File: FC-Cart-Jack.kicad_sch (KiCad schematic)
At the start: 5 parts, among them J1 ToCartridge, J2 ToConsole, J3 AudioJack3_SwitchTR, U1 LM321

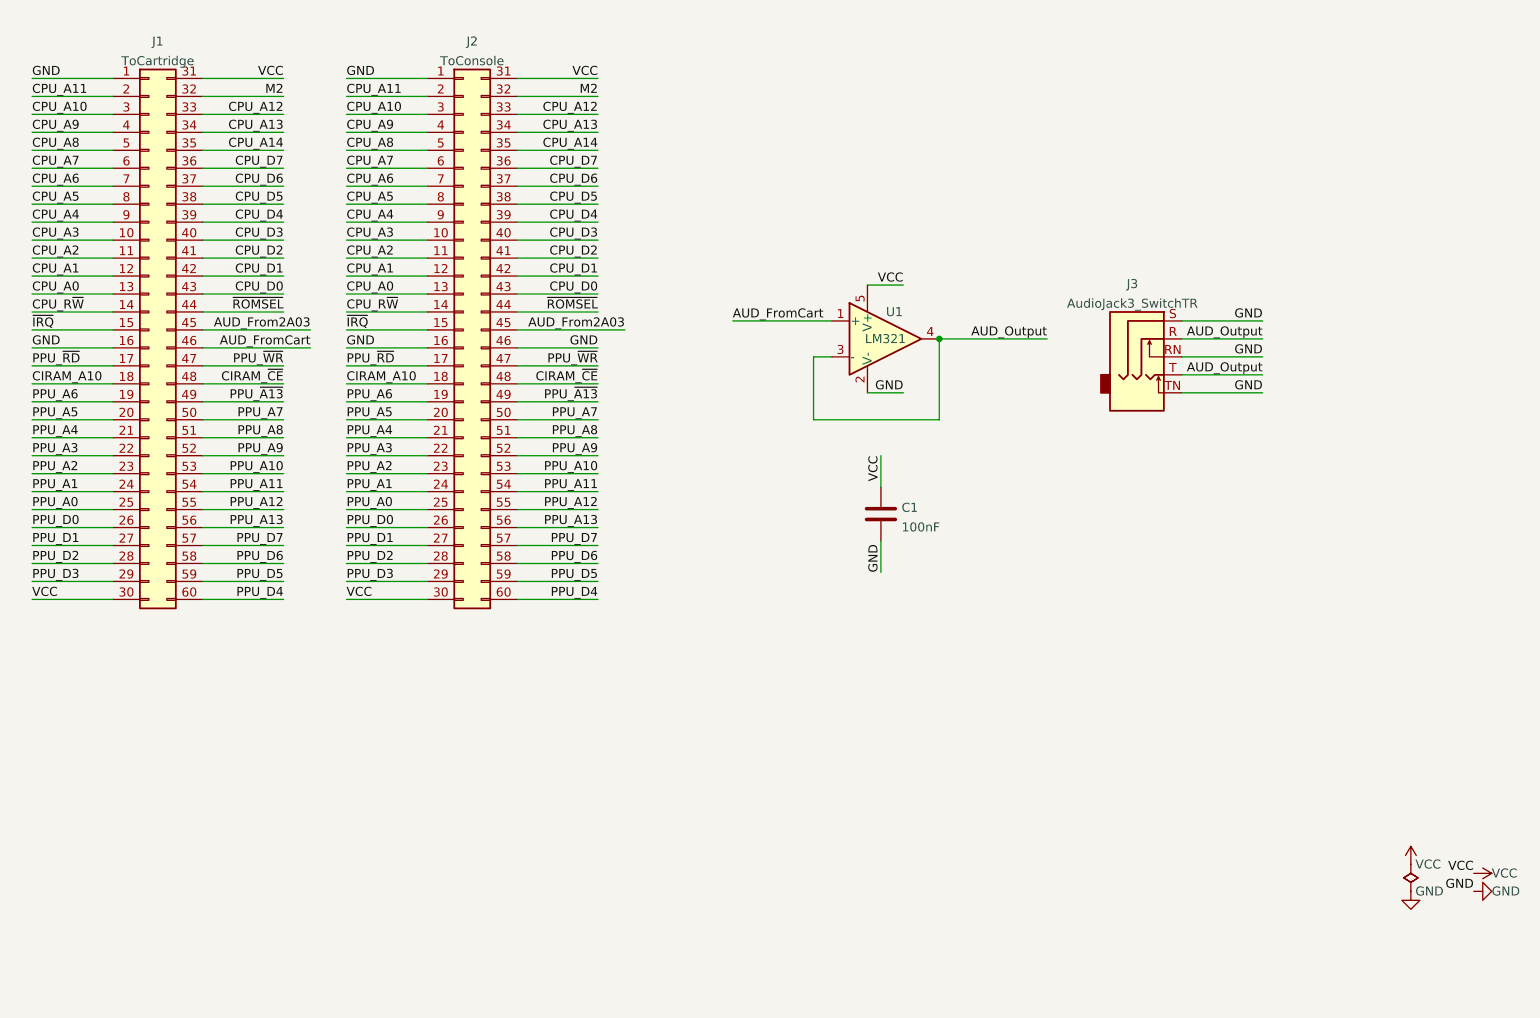
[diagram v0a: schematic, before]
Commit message: Update to KiCad 6.0
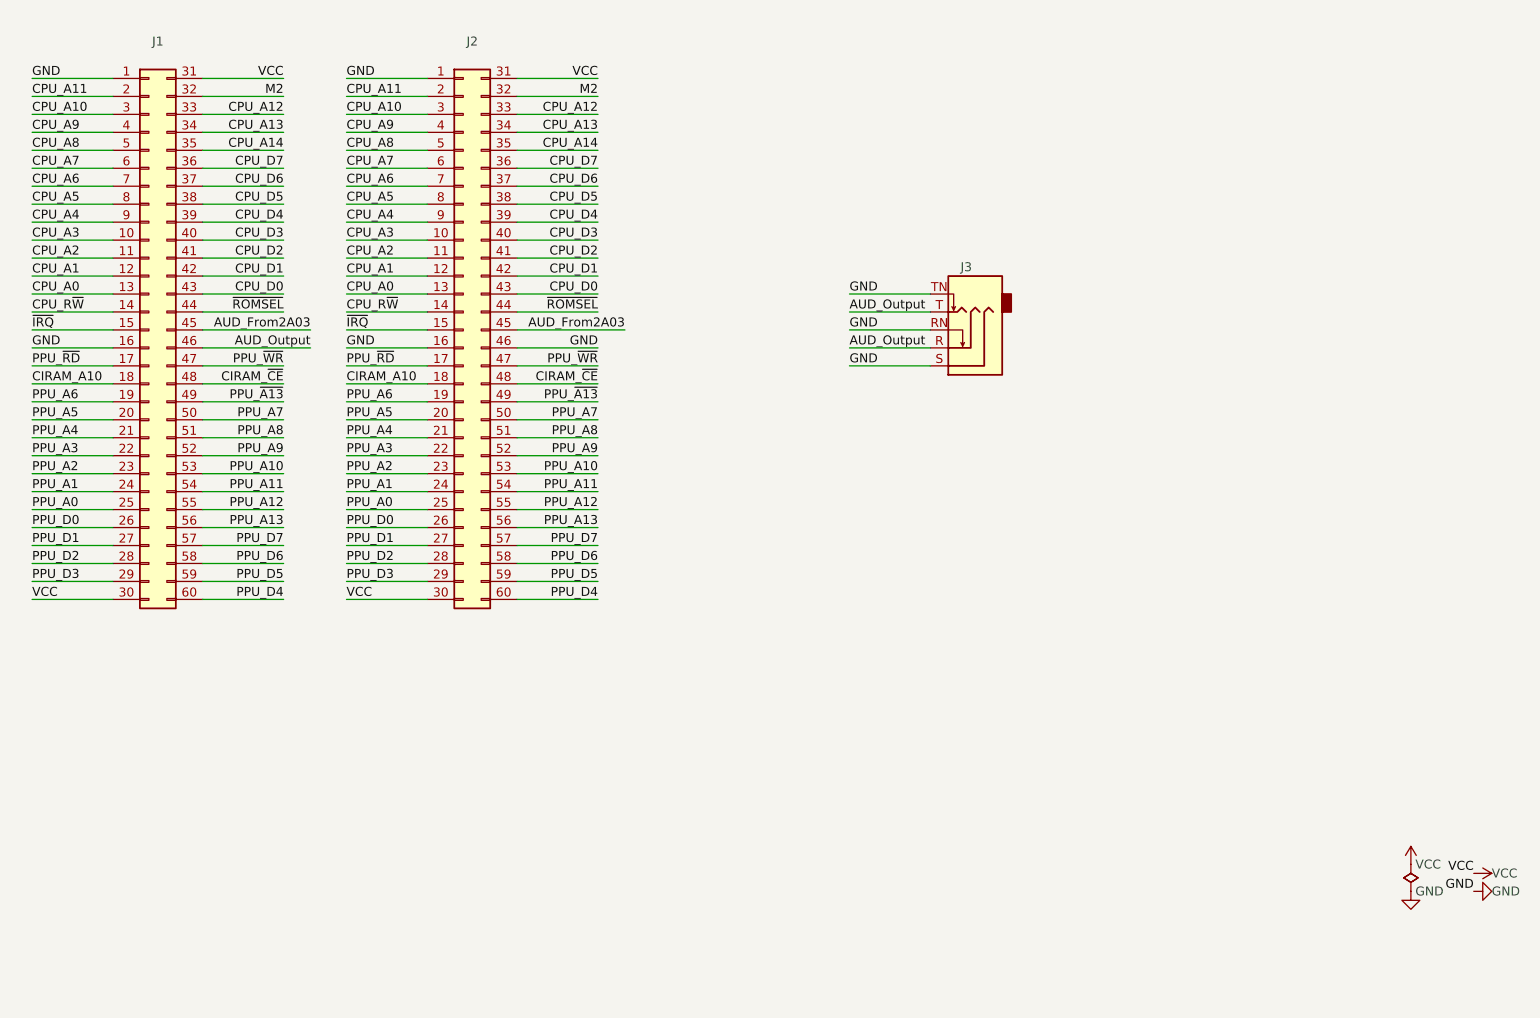
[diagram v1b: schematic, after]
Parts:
- removed C1: 100nF, Capacitor_SMD:C_0805_2012Metric, symbol Device:C
- removed U1: LM321, Package_TO_SOT_SMD:SOT-23-5, symbol Amplifier_Operational:LM321
- J1: value ToCartridge -> (none); footprint custom footprints:card edge -> (none)
- J2: value ToConsole -> (none); footprint custom footprints:HVC-TGROM-01 -> (none)
- J3: value AudioJack3_SwitchTR -> (none); footprint custom footprints:SJ1-3524NG -> (none)
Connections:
- net AUD_FromCart is gone; now on net AUD_Output: J1.46 (Pin_46)
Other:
- moved on the sheet: J3

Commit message: Leave audio out floating
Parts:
- J1: value (none) -> ToCartridge; footprint (none) -> FC-Cart-Jack:card edge
- J2: value (none) -> ToConsole; footprint (none) -> FC-Cart-Jack:HVC-TGROM-01
- J3: value (none) -> ~; footprint (none) -> FC-Cart-Jack:SJ1-3524NG
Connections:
- net GND: no longer J2.46 (Pin_46)
- net AUD_From2A03 renamed AUD_2A03
- no-connect marks 0 -> 1
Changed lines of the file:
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@@
   (title_block
     (title "FC Cartridge Audio Jack")
-    (date "2022-08-13")
-    (rev "0.0.4")
+    (date "2022-11-14")
+    (rev "0.0.5")
     (company "Persune")
   )
+  (no_connect (at 97.79 60.96))
   (wire (pts (xy 17.78 73.66) (xy 29.21 73.66))
     (stroke (width 0) (type default) (color 0 0 0 0))
   )
+  (wire (pts (xy 41.91 58.42) (xy 53.34 58.42))
+    (stroke (width 0) (type default) (color 0 0 0 0))
+  )
   (wire (pts (xy 17.78 71.12) (xy 29.21 71.12))
     (stroke (width 0) (type default) (color 0 0 0 0))
@@
     (stroke (width 0) (type default) (color 0 0 0 0))
   )
+  (wire (pts (xy 86.36 58.42) (xy 97.79 58.42))
+    (stroke (width 0) (type default) (color 0 0 0 0))
+  )
   (wire (pts (xy 62.23 53.34) (xy 73.66 53.34))
     (stroke (width 0) (type default) (color 0 0 0 0))
   )
-  (wire (pts (xy 86.36 58.42) (xy 101.6 58.42))
-    (stroke (width 0) (type default) (color 0 0 0 0))
-  )
   (wire (pts (xy 144.78 55.88) (xy 133.35 55.88))
     (stroke (width 0) (type default) (color 0 0 0 0))
@@
     (stroke (width 0) (type default) (color 0 0 0 0))
   )
-  (wire (pts (xy 41.91 60.96) (xy 57.15 60.96))
-    (stroke (width 0) (type default) (color 0 0 0 0))
-  )
   (wire (pts (xy 41.91 63.5) (xy 53.34 63.5))
     (stroke (width 0) (type default) (color 0 0 0 0))
@@
     (stroke (width 0) (type default) (color 0 0 0 0))
   )
-  (wire (pts (xy 41.91 58.42) (xy 57.15 58.42))
-    (stroke (width 0) (type default) (color 0 0 0 0))
-  )
   (wire (pts (xy 62.23 78.74) (xy 73.66 78.74))
     (stroke (width 0) (type default) (color 0 0 0 0))
@@
     (stroke (width 0) (type default) (color 0 0 0 0))
   )
+  (wire (pts (xy 41.91 60.96) (xy 53.34 60.96))
+    (stroke (width 0) (type default) (color 0 0 0 0))
+  )
   (wire (pts (xy 17.78 43.18) (xy 29.21 43.18))
     (stroke (width 0) (type default) (color 0 0 0 0))
@@
     (effects (font (size 1.27 1.27)) (justify right bottom))
   )
-  (label "AUD_From2A03" (at 101.6 58.42 180)
+  (label "AUD_2A03" (at 97.79 58.42 180)
     (effects (font (size 1.27 1.27)) (justify right bottom))
   )
@@
     (effects (font (size 1.27 1.27)) (justify left bottom))
   )
-  (label "AUD_From2A03" (at 57.15 58.42 180)
+  (label "AUD_2A03" (at 53.34 58.42 180)
     (effects (font (size 1.27 1.27)) (justify right bottom))
   )
@@
     (effects (font (size 1.27 1.27)) (justify left bottom))
   )
-  (label "AUD_Output" (at 57.15 60.96 180)
+  (label "AUD_Output" (at 53.34 60.96 180)
     (effects (font (size 1.27 1.27)) (justify right bottom))
   )
@@
   (label "PPU_A4" (at 17.78 73.66 0)
     (effects (font (size 1.27 1.27)) (justify left bottom))
-  )
-  (label "GND" (at 97.79 60.96 180)
-    (effects (font (size 1.27 1.27)) (justify right bottom))
   )
   (label "VCC" (at 53.34 22.86 180)
@@
     (in_bom yes) (on_board yes) (fields_autoplaced)
     (property "Reference" "J1" (id 0) (at 35.56 17.6235 0))
-    (property "Value" "" (id 1) (at 35.56 20.3986 0))
-    (property "Footprint" "" (id 2) (at 34.29 58.42 0)
+    (property "Value" "ToCartridge" (id 1) (at 35.56 20.3986 0))
+    (property "Footprint" "FC-Cart-Jack:card edge" (id 2) (at 34.29 58.42 0)
       (effects (font (size 1.27 1.27)) hide)
     )
@@
     (in_bom yes) (on_board yes)
     (property "Reference" "J3" (id 0) (at 149.86 49.53 0))
-    (property "Value" "" (id 1) (at 152.4 48.26 0)
+    (property "Value" "~" (id 1) (at 152.4 48.26 0)
       (effects (font (size 1.27 1.27)) hide)
     )
-    (property "Footprint" "" (id 2) (at 149.86 60.96 0)
+    (property "Footprint" "FC-Cart-Jack:SJ1-3524NG" (id 2) (at 149.86 60.96 0)
       (effects (font (size 1.27 1.27)) hide)
     )
@@
     (in_bom yes) (on_board yes) (fields_autoplaced)
     (property "Reference" "J2" (id 0) (at 80.01 17.6235 0))
-    (property "Value" "" (id 1) (at 80.01 20.3986 0))
-    (property "Footprint" "" (id 2) (at 78.74 58.42 0)
+    (property "Value" "ToConsole" (id 1) (at 80.01 20.3986 0))
+    (property "Footprint" "FC-Cart-Jack:HVC-TGROM-01" (id 2) (at 78.74 58.42 0)
       (effects (font (size 1.27 1.27)) hide)
     )

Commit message: Optionally terminate audio with 100K resistor
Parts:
- added R1: 100K, Resistor_SMD:R_0805_2012Metric_Pad1.20x1.40mm_HandSolder, symbol Device:R
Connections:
- net GND: now also R1.2
- net AUD_RF: now reaches J2.46 (Pin_46)
- net AUD_RF: now also R1.1
- no-connect marks 1 -> 0
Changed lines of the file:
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@@
     (title "FC Cartridge Audio Jack")
     (date "2022-11-14")
-    (rev "0.0.5")
+    (rev "0.0.6")
     (company "Persune")
   )
-  (no_connect (at 97.79 60.96))
   (wire (pts (xy 17.78 73.66) (xy 29.21 73.66))
     (stroke (width 0) (type default) (color 0 0 0 0))
@@
     (stroke (width 0) (type default) (color 0 0 0 0))
   )
+  (wire (pts (xy 152.4 71.12) (xy 163.83 71.12))
+    (stroke (width 0) (type default) (color 0 0 0 0))
+  )
   (wire (pts (xy 41.91 48.26) (xy 53.34 48.26))
     (stroke (width 0) (type default) (color 0 0 0 0))
@@
     (stroke (width 0) (type default) (color 0 0 0 0))
   )
+  (wire (pts (xy 133.35 71.12) (xy 144.78 71.12))
+    (stroke (width 0) (type default) (color 0 0 0 0))
+  )
   (wire (pts (xy 17.78 48.26) (xy 29.21 48.26))
     (stroke (width 0) (type default) (color 0 0 0 0))
@@
     (effects (font (size 1.27 1.27)) (justify left bottom))
   )
+  (label "GND" (at 163.83 71.12 180)
+    (effects (font (size 1.27 1.27)) (justify right bottom))
+  )
   (label "PPU_A0" (at 17.78 83.82 0)
     (effects (font (size 1.27 1.27)) (justify left bottom))
@@
   )
   (label "PPU_D4" (at 53.34 96.52 180)
+    (effects (font (size 1.27 1.27)) (justify right bottom))
+  )
+  (label "AUD_RF" (at 133.35 71.12 0)
+    (effects (font (size 1.27 1.27)) (justify left bottom))
+  )
+  (label "AUD_RF" (at 97.79 60.96 180)
     (effects (font (size 1.27 1.27)) (justify right bottom))
   )
@@
     )
     (pin "1")
+  )
+  (symbol (lib_id "Device:R") (at 148.59 71.12 90) (unit 1)
+    (in_bom yes) (on_board yes)
+    (property "Reference" "R1" (id 0) (at 148.59 68.58 90))
+    (property "Value" "100K" (id 1) (at 148.59 71.12 90))
+    (property "Footprint" "Resistor_SMD:R_0805_2012Metric_Pad1.20x1.40mm_HandSolder" (id 2) (at 148.59 72.898 90)
+      (effects (font (size 1.27 1.27)) hide)
+    )
+    (property "Datasheet" "~" (id 3) (at 148.59 71.12 0)
+      (effects (font (size 1.27 1.27)) hide)
+    )
+    (pin "1")
+    (pin "2")
   )
   (symbol (lib_id "Connector_Generic:Conn_02x30_Top_Bottom") (at 34.29 58.42 0) (unit 1)
@@
       (reference "J3") (unit 1) (value "~") (footprint "FC-Cart-Jack:SJ1-3524NG")
     )
-  )
+    (path "/53e270ac-224a-4586-a55a-ff444842f43e"
+      (reference "R1") (unit 1) (value "100K") (footprint "Resistor_SMD:R_0805_2012Metric_Pad1.20x1.40mm_HandSolder")
+    )
+  )

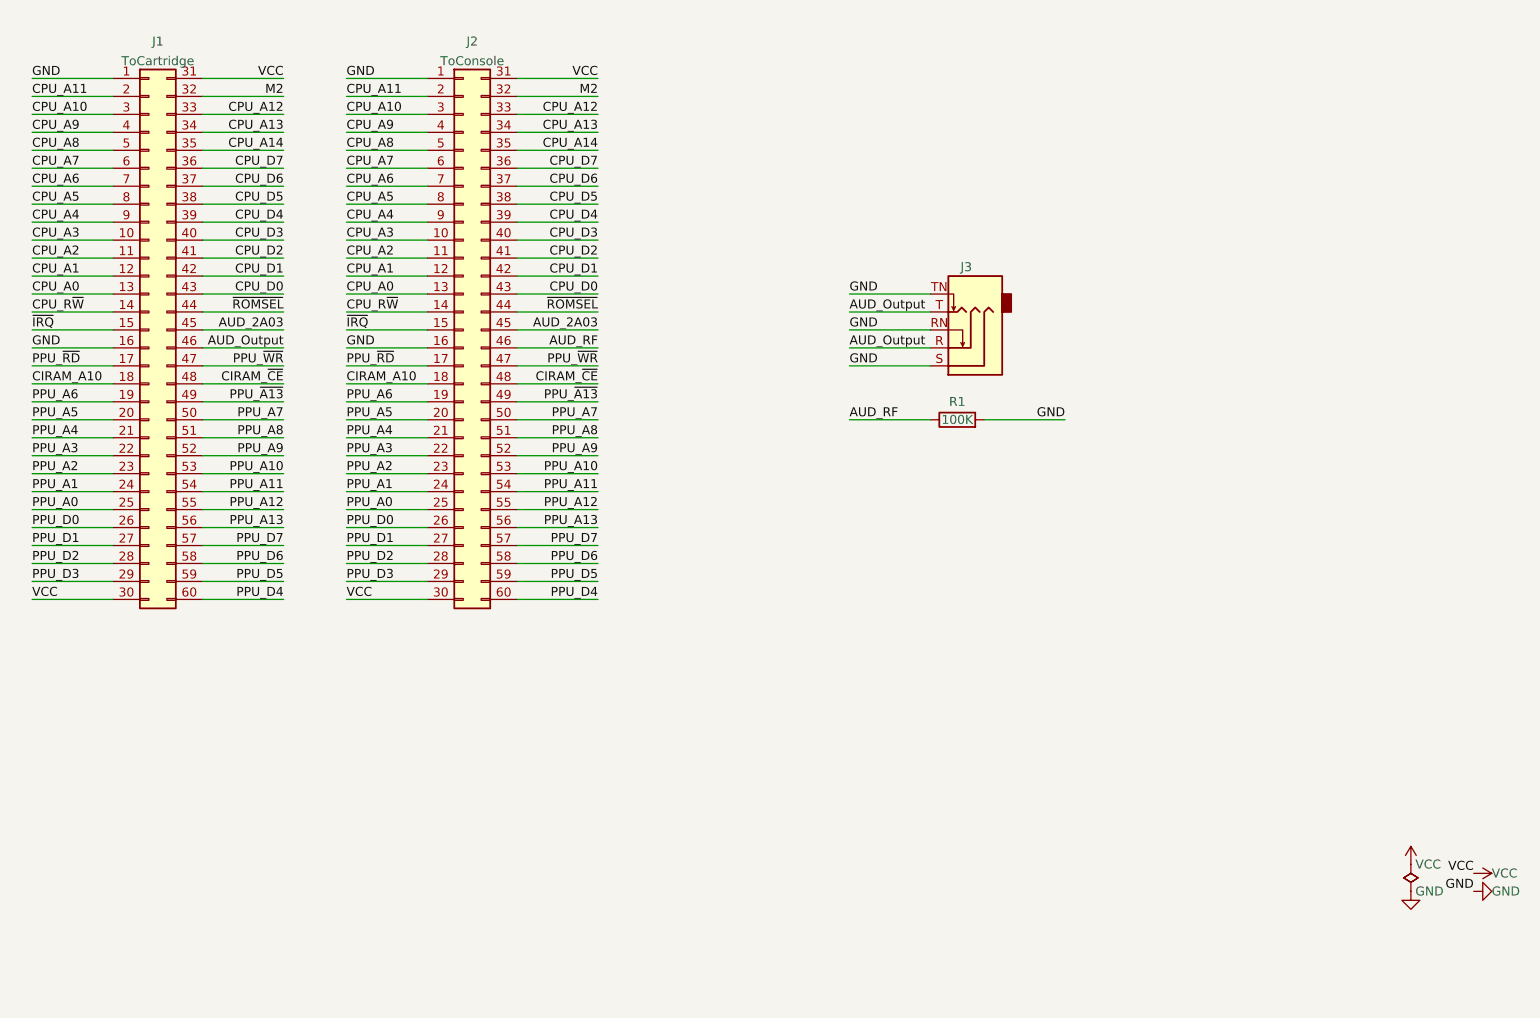
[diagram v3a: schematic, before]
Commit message: Add new buffer circuit
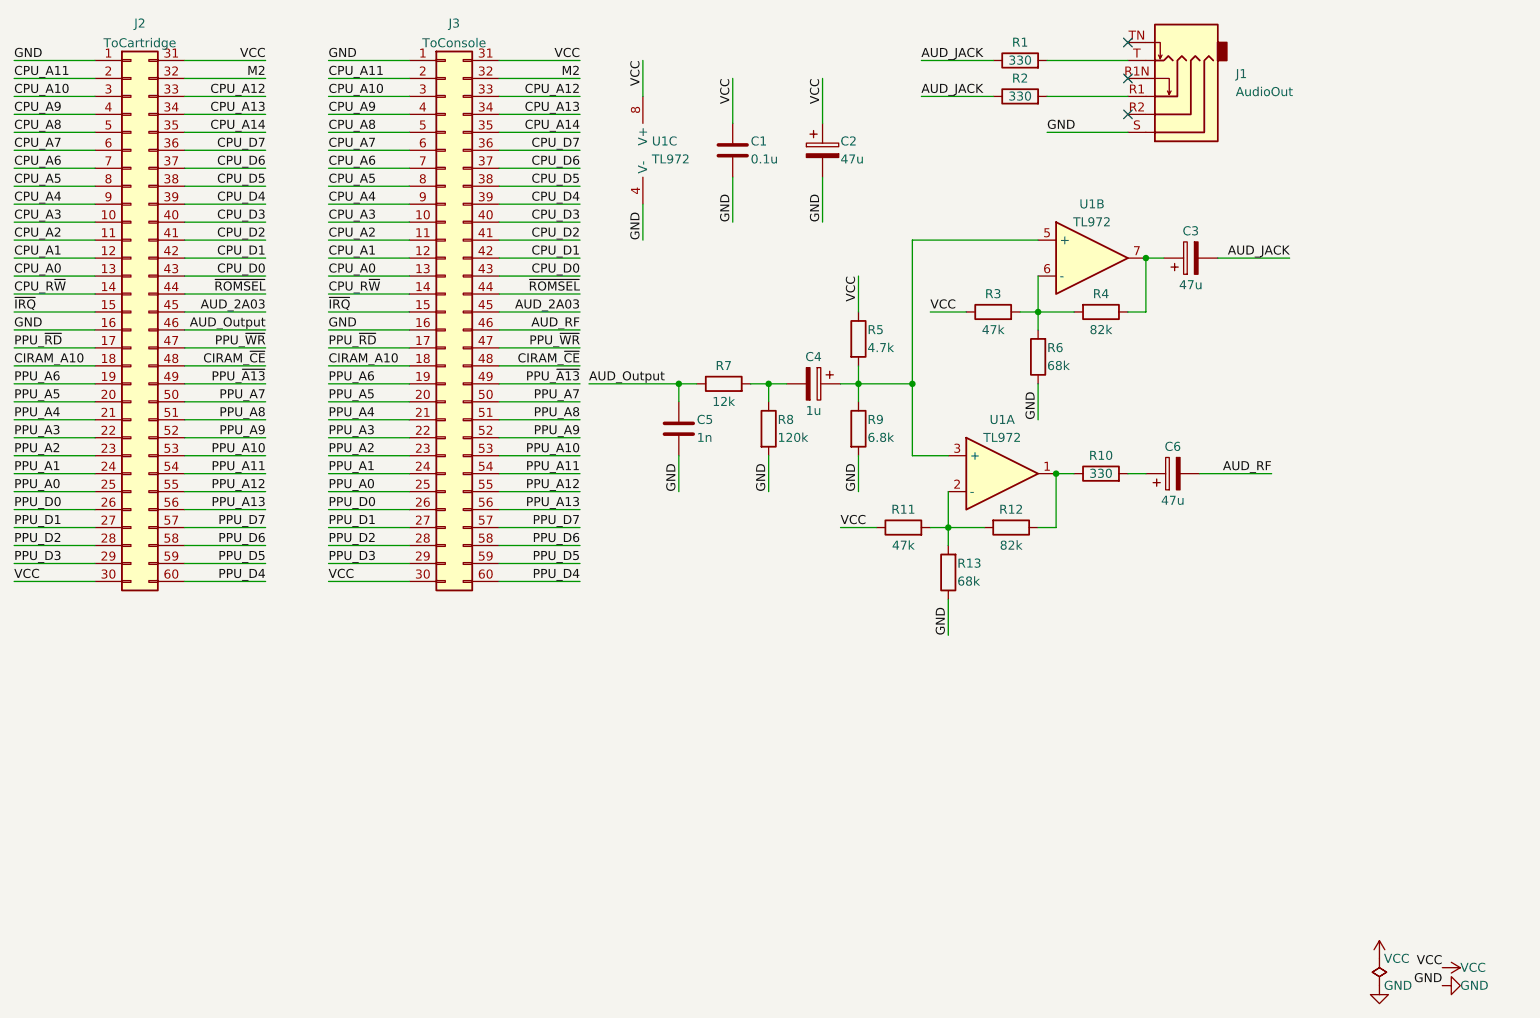
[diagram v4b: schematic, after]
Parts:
- removed J3: ~, FC-Cart-Jack:SJ1-3524NG, symbol Connector:AudioJack3_SwitchTR
- added C1: 0.1u, Capacitor_SMD:C_0805_2012Metric, symbol Device:C
- added C2, C3, C6: 47u, Capacitor_SMD:CP_Elec_5x5.4, symbol Device:C_Polarized
- added C4: 1u, Capacitor_SMD:CP_Elec_4x5.4, symbol Device:C_Polarized
- added C5: 1n, Capacitor_SMD:C_0805_2012Metric, symbol Device:C
- added J1: AudioOut, FC-Cart-Jack:Jack_3.5mm_PJ-342B-TX-SMT, symbol Connector_Audio:AudioJack4_SwitchTR1
- added R10, R2: 330, Resistor_SMD:R_0805_2012Metric, symbol Device:R
- added R11, R3: 47k, Resistor_SMD:R_0805_2012Metric, symbol Device:R
- added R12, R4: 82k, Resistor_SMD:R_0805_2012Metric, symbol Device:R
- added R13, R6: 68k, Resistor_SMD:R_0805_2012Metric, symbol Device:R
- added R5: 4.7k, Resistor_SMD:R_0805_2012Metric, symbol Device:R
- added R7: 12k, Resistor_SMD:R_0805_2012Metric, symbol Device:R
- added R8: 120k, Resistor_SMD:R_0805_2012Metric, symbol Device:R
- added R9: 6.8k, Resistor_SMD:R_0805_2012Metric, symbol Device:R
- added U1: TL972, Package_SO:SO-8_3.9x4.9mm_P1.27mm, symbol Device:Opamp_Dual
- J2: renamed from J1; footprint FC-Cart-Jack:card edge -> FC-Cart-Jack:FC_CONN_F
- R1: value 100K -> 330; footprint Resistor_SMD:R_0805_2012Metric_Pad1.20x1.40mm_HandSolder -> Resistor_SMD:R_0805_2012Metric
- renumbered J2 to J3
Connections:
- net AUD_Output: now also C5.1, R7.1
- net AUD_RF: now also C6.2; no longer R1.1
- net GND: now also C1.2, C2.2, C5.2, J1.S, R13.1, R6.1, R8.2, R9.2, U1.4 (V-); no longer R1.2
- net VCC: now also C1.1, C2.1, R11.1, R3.1, R5.1, U1.8 (V+)
- new net: C4.2, R7.2, R8.1
- new net: C6.1, R10.2
- new net: C4.1, R5.2, R9.1, U1.3 (+), U1.5 (+)
- new net: C3.1, R4.1, U1.7
- new net: R3.2, R4.2, R6.2, U1.6 (-)
- new net: R10.1, R12.1, U1.1
- new net: R11.2, R12.2, R13.2, U1.2 (-)
- new net: J1.R1, R2.2
- new net: J1.T, R1.2
- new net AUD_JACK: C3.2, R1.1, R2.1
- no-connect marks 0 -> 3
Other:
- moved on the sheet: J2, J3
